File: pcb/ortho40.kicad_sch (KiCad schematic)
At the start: 1 part

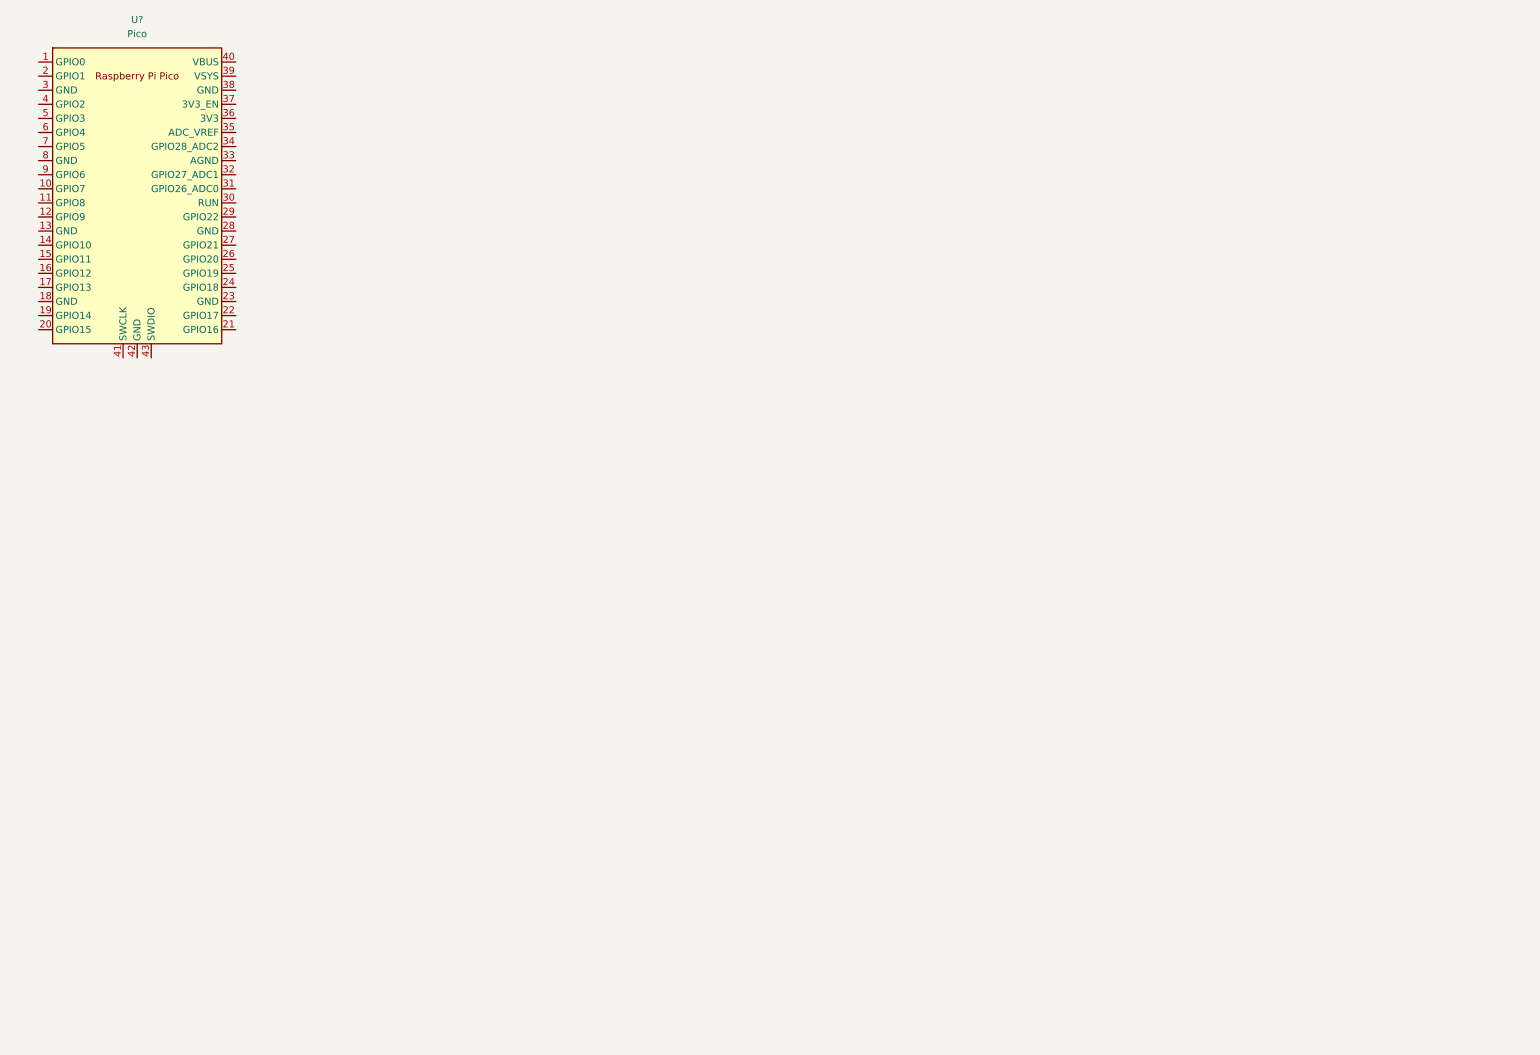
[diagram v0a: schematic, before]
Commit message: Finish Matrix + Start RP2040 setup
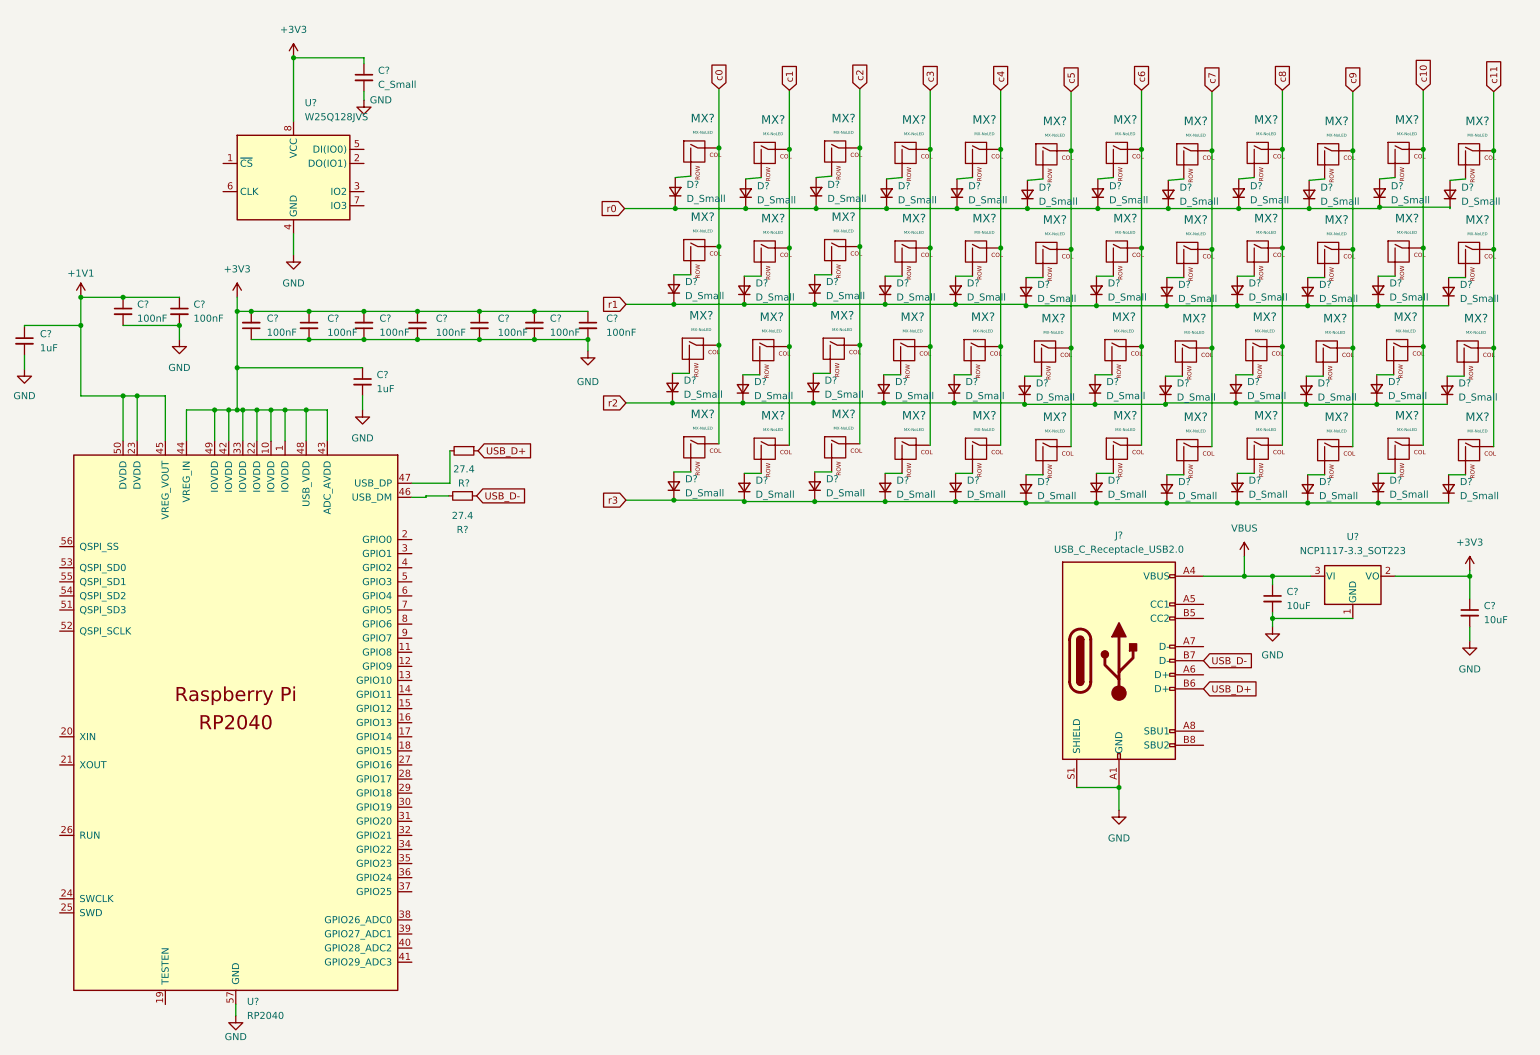
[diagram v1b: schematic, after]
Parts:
- removed U?: Pico, RPi_Pico:RPi_Pico_SMD_TH, symbol MCU_RaspberryPi_and_Boards:Pico
- added C? (x9): 100nF, symbol Device:C_Small
- added C? (x2): 1uF, symbol Device:C_Small
- added C? (x2): 10uF, symbol Device:C_Small
- added C?: C_Small, symbol Device:C_Small
- added D? (x48): D_Small, symbol Device:D_Small
- added J?: USB_C_Receptacle_USB2.0, symbol Connector:USB_C_Receptacle_USB2.0
- added MX? (x48): MX-NoLED, symbol MX_Alps_Hybrid:MX-NoLED
- added R? (x2): 27.4, symbol Device:R_Small
- added U?: NCP1117-3.3_SOT223, Package_TO_SOT_SMD:SOT-223-3_TabPin2, symbol Regulator_Linear:NCP1117-3.3_SOT223
- added U?: RP2040, RP2040_minimal:RP2040-QFN-56, symbol MCU_RaspberryPi_and_Boards:RP2040
- added U?: W25Q128JVS, Package_SO:SOIC-8_5.23x5.23mm_P1.27mm, symbol Memory_Flash:W25Q128JVS
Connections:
- new net: R?.2, U?.47 (USB_DP)
- new net: D?.2 (A), MX?.2 (ROW) (x48)
- new net: R?.2, U?.46 (USB_DM)
- new net +1V1: C?.1, C?.1, C?.1, U?.23 (DVDD), U?.45 (VREG_VOUT), U?.50 (DVDD)
- new net +3V3: C?.1, C?.1, C?.1, C?.1, C?.1, C?.1, C?.1, C?.2, C?.2, C?.2, U?.1 (IOVDD), U?.10 (IOVDD), U?.2 (VO), U?.22 (IOVDD), U?.33 (IOVDD), U?.42 (IOVDD), U?.43 (ADC_AVDD), U?.44 (VREG_IN), U?.48 (USB_VDD), U?.49 (IOVDD), U?.8 (VCC)
- new net GND: C?.1, C?.1, C?.1, C?.2, C?.2, C?.2, C?.2, C?.2, C?.2, C?.2, C?.2, C?.2, C?.2, C?.2, J?.A1 (GND), J?.A12 (GND), J?.B1 (GND), J?.B12 (GND), J?.S1 (SHIELD), U?.1 (GND), U?.4 (GND), U?.57 (GND)
- new net USB_D+: J?.B6 (D+), R?.1
- new net USB_D-: J?.B7 (D-), R?.1
- new net VBUS: C?.1, J?.A4 (VBUS), J?.A9 (VBUS), J?.B4 (VBUS), J?.B9 (VBUS), U?.3 (VI)
- new net c0: MX?.1 (COL), MX?.1 (COL), MX?.1 (COL), MX?.1 (COL)
- new net c1: MX?.1 (COL), MX?.1 (COL), MX?.1 (COL), MX?.1 (COL)
- new net c10: MX?.1 (COL), MX?.1 (COL), MX?.1 (COL), MX?.1 (COL)
- new net c11: MX?.1 (COL), MX?.1 (COL), MX?.1 (COL), MX?.1 (COL)
- new net c2: MX?.1 (COL), MX?.1 (COL), MX?.1 (COL), MX?.1 (COL)
- new net c3: MX?.1 (COL), MX?.1 (COL), MX?.1 (COL), MX?.1 (COL)
- new net c4: MX?.1 (COL), MX?.1 (COL), MX?.1 (COL), MX?.1 (COL)
- new net c5: MX?.1 (COL), MX?.1 (COL), MX?.1 (COL), MX?.1 (COL)
- new net c6: MX?.1 (COL), MX?.1 (COL), MX?.1 (COL), MX?.1 (COL)
- new net c7: MX?.1 (COL), MX?.1 (COL), MX?.1 (COL), MX?.1 (COL)
- new net c8: MX?.1 (COL), MX?.1 (COL), MX?.1 (COL), MX?.1 (COL)
- new net c9: MX?.1 (COL), MX?.1 (COL), MX?.1 (COL), MX?.1 (COL)
- new net r0: D?.1 (K), D?.1 (K), D?.1 (K), D?.1 (K), D?.1 (K), D?.1 (K), D?.1 (K), D?.1 (K), D?.1 (K), D?.1 (K), D?.1 (K), D?.1 (K)
- new net r1: D?.1 (K), D?.1 (K), D?.1 (K), D?.1 (K), D?.1 (K), D?.1 (K), D?.1 (K), D?.1 (K), D?.1 (K), D?.1 (K), D?.1 (K), D?.1 (K)
- new net r2: D?.1 (K), D?.1 (K), D?.1 (K), D?.1 (K), D?.1 (K), D?.1 (K), D?.1 (K), D?.1 (K), D?.1 (K), D?.1 (K), D?.1 (K), D?.1 (K)
- new net r3: D?.1 (K), D?.1 (K), D?.1 (K), D?.1 (K), D?.1 (K), D?.1 (K), D?.1 (K), D?.1 (K), D?.1 (K), D?.1 (K), D?.1 (K), D?.1 (K)

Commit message: Schematic done
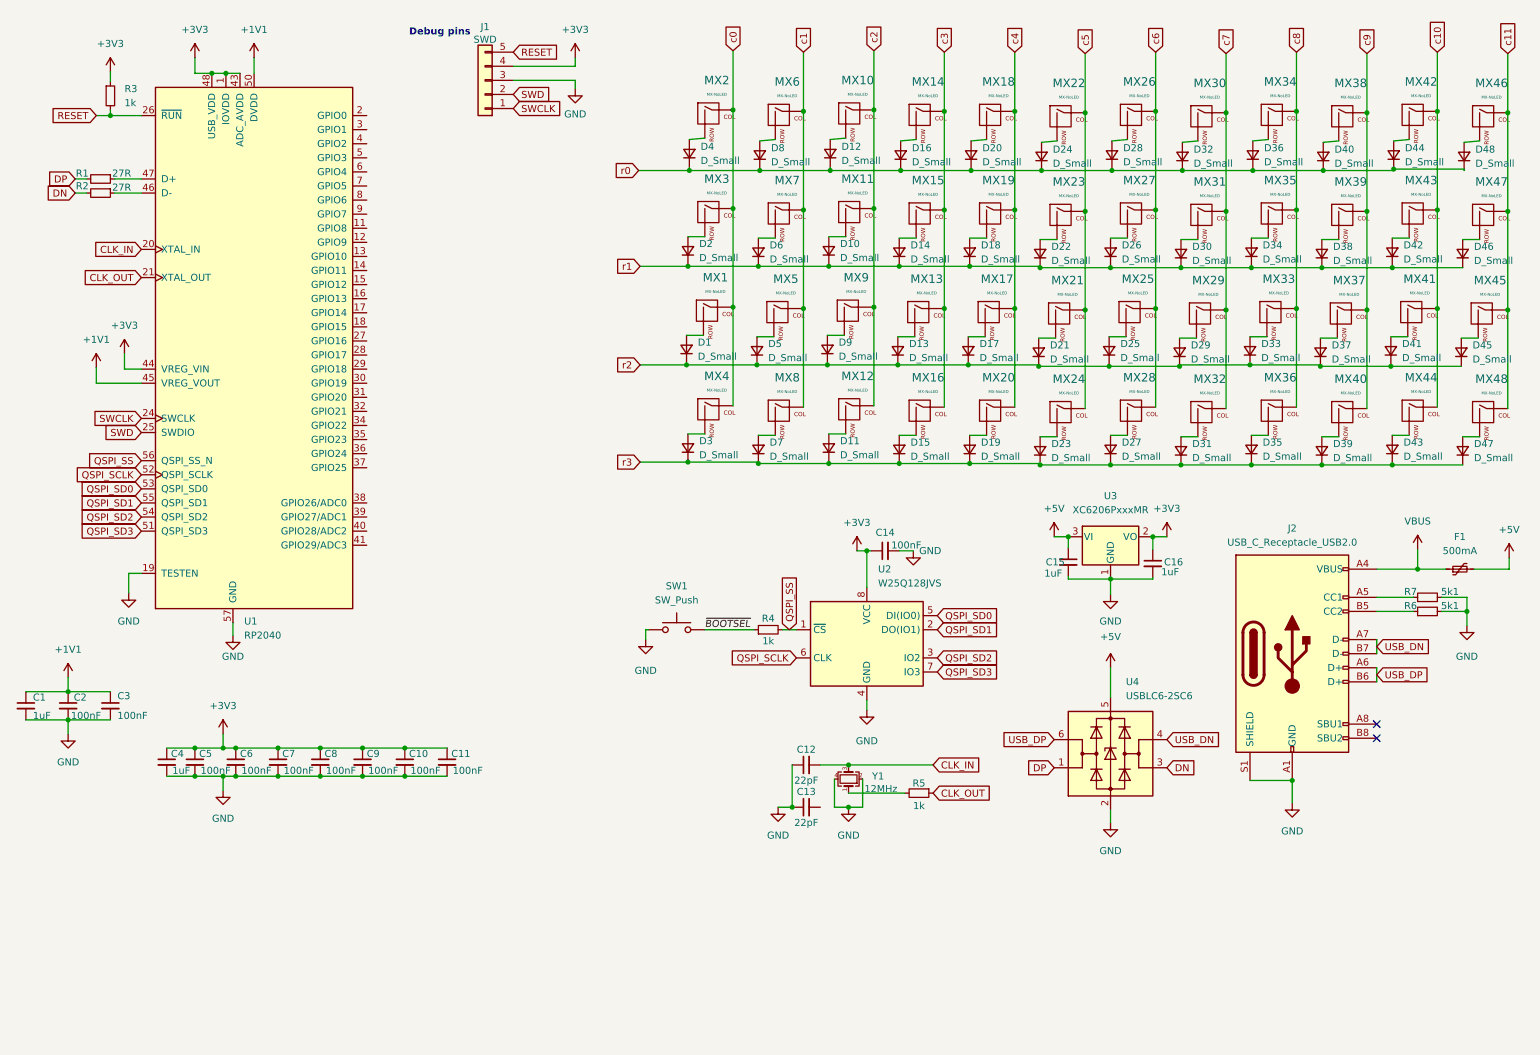
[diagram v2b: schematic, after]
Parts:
- removed C? (x9): 100nF, symbol Device:C_Small
- removed C? (x2): 1uF, symbol Device:C_Small
- removed C? (x2): 10uF, symbol Device:C_Small
- removed U?: NCP1117-3.3_SOT223, Package_TO_SOT_SMD:SOT-223-3_TabPin2, symbol Regulator_Linear:NCP1117-3.3_SOT223
- removed U?: RP2040, RP2040_minimal:RP2040-QFN-56, symbol MCU_RaspberryPi_and_Boards:RP2040
- added C1, C15, C16, C4: 1uF, Capacitor_SMD:C_0402_1005Metric, symbol Device:C_Small
- added C10, C11, C2, C3, C5, C6, C7, C8, C9: 100nF, Capacitor_SMD:C_0402_1005Metric, symbol Device:C_Small
- added C12, C13: 22pF, Capacitor_SMD:C_0402_1005Metric, symbol Device:C_Small
- added F1: 500mA, Fuse:Fuse_1206_3216Metric, symbol Device:Polyfuse_Small
- added J1: SWD, Connector_PinSocket_2.54mm:PinSocket_1x05_P2.54mm_Vertical, symbol Connector_Generic:Conn_01x05
- added R3, R4, R5: 1k, Resistor_SMD:R_4020_10251Metric, symbol Device:R_Small
- added R6, R7: 5k1, Resistor_SMD:R_4020_10251Metric, symbol Device:R_Small
- added SW1: SW_Push, Connector_PinHeader_2.54mm:PinHeader_1x02_P2.54mm_Vertical, symbol Switch:SW_Push
- added U1: RP2040, Footprints:RP2040-QFN-56, symbol Sleep-lib:RP2040
- added U3: XC6206PxxxMR, Package_TO_SOT_SMD:SOT-23, symbol Regulator_Linear:XC6206PxxxMR
- added U4: USBLC6-2SC6, Package_TO_SOT_SMD:SOT-23-6, symbol Power_Protection:USBLC6-2SC6
- added Y1: 12MHz, Crystal:Crystal_SMD_3225-4Pin_3.2x2.5mm, symbol Device:Crystal_GND24_Small
- C14: renamed from C?; value C_Small -> 100nF; footprint (none) -> Capacitor_SMD:C_0402_1005Metric
- D1, D10, D11, D12, D13, D14, D15, D16, D17, D18, D19, D2, D20, D21, D22, D23, D24, D25, D26, D27, D28, D29, D3, D30, D31, D32, D33, D34, D35, D36, D37, D38, D39, D4, D40, D41, D42, D43, D44, D45, D46, D47, D48, D5, D6, D7, D8, D9: renamed from D?; footprint (none) -> Diode_SMD:D_0201_0603Metric
- J2: renamed from J?; footprint (none) -> Connector_USB:USB_C_Receptacle_HRO_TYPE-C-31-M-12
- MX1, MX10, MX11, MX12, MX13, MX14, MX15, MX16, MX17, MX18, MX19, MX2, MX20, MX21, MX22, MX23, MX24, MX25, MX26, MX27, MX28, MX29, MX3, MX30, MX31, MX32, MX33, MX34, MX35, MX36, MX37, MX38, MX39, MX4, MX40, MX41, MX42, MX43, MX44, MX45, MX46, MX47, MX48, MX5, MX6, MX7, MX8, MX9: renamed from MX?; footprint (none) -> MX_Alps_Hybrid:MX-1U-NoLED
- R1, R2: renamed from R?; value 27.4 -> 27R; footprint (none) -> Resistor_SMD:R_4020_10251Metric
- gave numbers to parts that had none: 1
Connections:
- net +1V1: now also C1.1, C2.1, C3.1, U1.23 (DVDD), U1.45 (VREG_VOUT), U1.50 (DVDD)
- net +3V3: now also C10.1, C11.1, C16.1, C4.1, C5.1, C6.1, C7.1, C8.1, C9.1, J1.4 (Pin_4), R3.1, U1.1 (IOVDD), U1.10 (IOVDD), U1.22 (IOVDD), U1.33 (IOVDD), U1.42 (IOVDD), U1.43 (ADC_AVDD), U1.44 (VREG_VIN), U1.48 (USB_VDD), U1.49 (IOVDD), U3.2 (VO)
- net GND: now also C1.2, C10.2, C11.2, C12.1, C13.1, C15.2, C16.2, C2.2, C3.2, C4.2, C5.2, C6.2, C7.2, C8.2, C9.2, J1.3 (Pin_3), R6.2, R7.2, SW1.1, U1.19 (TESTEN), U1.57 (GND), U3.1 (GND), U4.2 (GND), Y1.2, Y1.4
- net VBUS: now also F1.1
- net DP: now reaches R1.2
- net DP: now also U4.1 (I/O1)
- net DN: now reaches R2.2
- net DN: now also U4.3 (I/O2)
- net at J2.A5 (CC1): now also R6.1
- net USB_DP: now reaches J2.A6 (D+)
- net USB_DP: now also J2.B6 (D+), U4.6 (I/O1)
- net USB_DN: now reaches J2.A7 (D-)
- net USB_DN: now also J2.B7 (D-), U4.4 (I/O2)
- net at J2.B5 (CC2): now also R7.1
- net QSPI_SS: now reaches U2.1 (~{CS})
- net QSPI_SS: now also R4.2, U1.56 (QSPI_SS_N)
- net QSPI_SD1: now reaches U2.2 (DO(IO1))
- net QSPI_SD1: now also U1.55 (QSPI_SD1)
- net QSPI_SD2: now reaches U2.3 (IO2)
- net QSPI_SD2: now also U1.54 (QSPI_SD2)
- net QSPI_SD0: now reaches U2.5 (DI(IO0))
- net QSPI_SD0: now also U1.53 (QSPI_SD0)
- net QSPI_SCLK: now reaches U2.6 (CLK)
- net QSPI_SCLK: now also U1.52 (QSPI_SCLK)
- net QSPI_SD3: now reaches U2.7 (IO3)
- net QSPI_SD3: now also U1.51 (QSPI_SD3)
- net USB_D+: no longer names the net of R1.1
- net USB_D+: now also U1.47 (D+); no longer J2.B6 (D+)
- net USB_D-: no longer names the net of R2.1
- net USB_D-: now also U1.46 (D-); no longer J2.B7 (D-)
- new net: R5.2, Y1.1
- new net +5V: C15.1, F1.2, U3.3 (VI), U4.5 (VBUS)
- new net CLK_IN: C12.2, U1.20 (XTAL_IN), Y1.3
- new net CLK_OUT: R5.1, U1.21 (XTAL_OUT)
- new net RESET: J1.5 (Pin_5), R3.2, U1.26 (~{RUN})
- new net SWCLK: J1.1 (Pin_1), U1.24 (SWCLK)
- new net SWD: J1.2 (Pin_2), U1.25 (SWDIO)
- new net ~{BOOTSEL}: R4.1, SW1.2
- no-connect marks 0 -> 2
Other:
- note added: "Debug pins"
- moved on the sheet: C14, D1, D10, D11, D12, D13, D14, D15, D16, D17, D18, D19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

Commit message: blobpain
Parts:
- added U?: ST7735_1.8inch, symbol kicub_keyboard_extras:ST7735_1.8inch
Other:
- moved on the sheet: C1, C10, C11, C2, C3, C4, C5, C6, C7, C8, C9

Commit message: Kindof finish pcb
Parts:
- D1: renamed from D4; footprint Diode_SMD:D_0201_0603Metric -> Diode_SMD:D_SOD-123
- D10: renamed from D32; footprint Diode_SMD:D_0201_0603Metric -> Diode_SMD:D_SOD-123
- D11: renamed from D40; footprint Diode_SMD:D_0201_0603Metric -> Diode_SMD:D_SOD-123
- D12: renamed from D48; footprint Diode_SMD:D_0201_0603Metric -> Diode_SMD:D_SOD-123
- D13: renamed from D2; footprint Diode_SMD:D_0201_0603Metric -> Diode_SMD:D_SOD-123
- D14: renamed from D10; footprint Diode_SMD:D_0201_0603Metric -> Diode_SMD:D_SOD-123
- D15: renamed from D6; footprint Diode_SMD:D_0201_0603Metric -> Diode_SMD:D_SOD-123
- D16: renamed from D14; footprint Diode_SMD:D_0201_0603Metric -> Diode_SMD:D_SOD-123
- D17: renamed from D18; footprint Diode_SMD:D_0201_0603Metric -> Diode_SMD:D_SOD-123
- D18: renamed from D26; footprint Diode_SMD:D_0201_0603Metric -> Diode_SMD:D_SOD-123
- D19: renamed from D34; footprint Diode_SMD:D_0201_0603Metric -> Diode_SMD:D_SOD-123
- D2: renamed from D12; footprint Diode_SMD:D_0201_0603Metric -> Diode_SMD:D_SOD-123
- D20: renamed from D42; footprint Diode_SMD:D_0201_0603Metric -> Diode_SMD:D_SOD-123
- D21: renamed from D22; footprint Diode_SMD:D_0201_0603Metric -> Diode_SMD:D_SOD-123
- D22: renamed from D30; footprint Diode_SMD:D_0201_0603Metric -> Diode_SMD:D_SOD-123
- D23: renamed from D38; footprint Diode_SMD:D_0201_0603Metric -> Diode_SMD:D_SOD-123
- D24: renamed from D46; footprint Diode_SMD:D_0201_0603Metric -> Diode_SMD:D_SOD-123
- D25: renamed from D1; footprint Diode_SMD:D_0201_0603Metric -> Diode_SMD:D_SOD-123
- D26: renamed from D9; footprint Diode_SMD:D_0201_0603Metric -> Diode_SMD:D_SOD-123
- D27: renamed from D5; footprint Diode_SMD:D_0201_0603Metric -> Diode_SMD:D_SOD-123
- D28: renamed from D13; footprint Diode_SMD:D_0201_0603Metric -> Diode_SMD:D_SOD-123
- D29: renamed from D17; footprint Diode_SMD:D_0201_0603Metric -> Diode_SMD:D_SOD-123
- D3: renamed from D8; footprint Diode_SMD:D_0201_0603Metric -> Diode_SMD:D_SOD-123
- D30: renamed from D25; footprint Diode_SMD:D_0201_0603Metric -> Diode_SMD:D_SOD-123
- D31: renamed from D33; footprint Diode_SMD:D_0201_0603Metric -> Diode_SMD:D_SOD-123
- D32: renamed from D41; footprint Diode_SMD:D_0201_0603Metric -> Diode_SMD:D_SOD-123
- D33: renamed from D21; footprint Diode_SMD:D_0201_0603Metric -> Diode_SMD:D_SOD-123
- D34: renamed from D29; footprint Diode_SMD:D_0201_0603Metric -> Diode_SMD:D_SOD-123
- D35: renamed from D37; footprint Diode_SMD:D_0201_0603Metric -> Diode_SMD:D_SOD-123
- D36: renamed from D45; footprint Diode_SMD:D_0201_0603Metric -> Diode_SMD:D_SOD-123
- D37: renamed from D3; footprint Diode_SMD:D_0201_0603Metric -> Diode_SMD:D_SOD-123
- D38: renamed from D11; footprint Diode_SMD:D_0201_0603Metric -> Diode_SMD:D_SOD-123
- D39: renamed from D7; footprint Diode_SMD:D_0201_0603Metric -> Diode_SMD:D_SOD-123
- D4: renamed from D16; footprint Diode_SMD:D_0201_0603Metric -> Diode_SMD:D_SOD-123
- D40: renamed from D15; footprint Diode_SMD:D_0201_0603Metric -> Diode_SMD:D_SOD-123
- D41: renamed from D19; footprint Diode_SMD:D_0201_0603Metric -> Diode_SMD:D_SOD-123
- D42: renamed from D27; footprint Diode_SMD:D_0201_0603Metric -> Diode_SMD:D_SOD-123
- D43: renamed from D35; footprint Diode_SMD:D_0201_0603Metric -> Diode_SMD:D_SOD-123
- D44: renamed from D43; footprint Diode_SMD:D_0201_0603Metric -> Diode_SMD:D_SOD-123
- D45: renamed from D23; footprint Diode_SMD:D_0201_0603Metric -> Diode_SMD:D_SOD-123
- D46: renamed from D31; footprint Diode_SMD:D_0201_0603Metric -> Diode_SMD:D_SOD-123
- D47: renamed from D39; footprint Diode_SMD:D_0201_0603Metric -> Diode_SMD:D_SOD-123
- D48: renamed from D47; footprint Diode_SMD:D_0201_0603Metric -> Diode_SMD:D_SOD-123
- D5: renamed from D20; footprint Diode_SMD:D_0201_0603Metric -> Diode_SMD:D_SOD-123
- D6: renamed from D28; footprint Diode_SMD:D_0201_0603Metric -> Diode_SMD:D_SOD-123
- D7: renamed from D36; footprint Diode_SMD:D_0201_0603Metric -> Diode_SMD:D_SOD-123
- D8: renamed from D44; footprint Diode_SMD:D_0201_0603Metric -> Diode_SMD:D_SOD-123
- D9: renamed from D24; footprint Diode_SMD:D_0201_0603Metric -> Diode_SMD:D_SOD-123
- R1: renamed from R3; footprint Resistor_SMD:R_4020_10251Metric -> Resistor_SMD:R_0402_1005Metric
- R2: renamed from R1; footprint Resistor_SMD:R_4020_10251Metric -> Resistor_SMD:R_0402_1005Metric
- R3: renamed from R2; footprint Resistor_SMD:R_4020_10251Metric -> Resistor_SMD:R_0402_1005Metric
- R4: renamed from R6; footprint Resistor_SMD:R_4020_10251Metric -> Resistor_SMD:R_0402_1005Metric
- R5: renamed from R7; footprint Resistor_SMD:R_4020_10251Metric -> Resistor_SMD:R_0402_1005Metric
- R6: renamed from R4; footprint Resistor_SMD:R_4020_10251Metric -> Resistor_SMD:R_0402_1005Metric
- R7: renamed from R5; footprint Resistor_SMD:R_4020_10251Metric -> Resistor_SMD:R_0402_1005Metric
- U5: renamed from U?; value ST7735_1.8inch -> ST7735S_1.8inch; footprint (none) -> Footprints:ST7735_1.8inch
- renumbered C14 to C1, C7 to C10, C8 to C11, C9 to C12, C10 to C13, C11 to C14, C12 to C15, C13 to C16, C15 to C2, C16 to C3, C1 to C4, C2 to C5, C3 to C6, C4 to C7, C5 to C8, C6 to C9, MX2 to MX1, MX38 to MX10, MX42 to MX11, MX46 to MX12, MX3 to MX13, MX7 to MX14, MX11 to MX15, MX15 to MX16, MX19 to MX17, MX23 to MX18, MX27 to MX19, MX6 to MX2, MX31 to MX20, MX35 to MX21, MX39 to MX22, MX43 to MX23, MX47 to MX24, MX1 to MX25, MX5 to MX26, MX9 to MX27, MX13 to MX28, MX17 to MX29, MX10 to MX3, MX21 to MX30, MX25 to MX31, MX29 to MX32, MX37 to MX34, MX41 to MX35, MX45 to MX36, MX4 to MX37, MX8 to MX38, MX12 to MX39, MX14 to MX4, MX16 to MX40, MX20 to MX41, MX24 to MX42, MX28 to MX43, MX32 to MX44, MX36 to MX45, MX40 to MX46, MX44 to MX47, MX18 to MX5, MX22 to MX6, MX26 to MX7, MX30 to MX8, MX34 to MX9, U3 to U2, U2 to U3
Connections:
- net +3V3: now also U5.1 (VCC)
- net GND: now also U5.2 (GND)
- net at R7.2, Y1.1: now also C16.2
- net LCD_SCK: now reaches U5.3 (SCLK)
- net LCD_TX: now reaches U5.4 (MOSI)
- net LCD_RX: now reaches U5.5 (MISO)
- net LCD_CS: now reaches U5.6 (CS)
- net LCD_RESET: now reaches U5.7 (~{RESET})
- net LCD_DC: now reaches U5.8 (DC)
- new net LCD_BACKLT: U5.9 (BLK)
- new net LCD_SDSEL: U5.10 (SDCS)
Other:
- moved on the sheet: D1, D10, D11, D12, D13, D14, D15, D16, D17, D18, D19, D2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
